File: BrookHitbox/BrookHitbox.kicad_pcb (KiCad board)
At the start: 2 copper layers, 15 parts

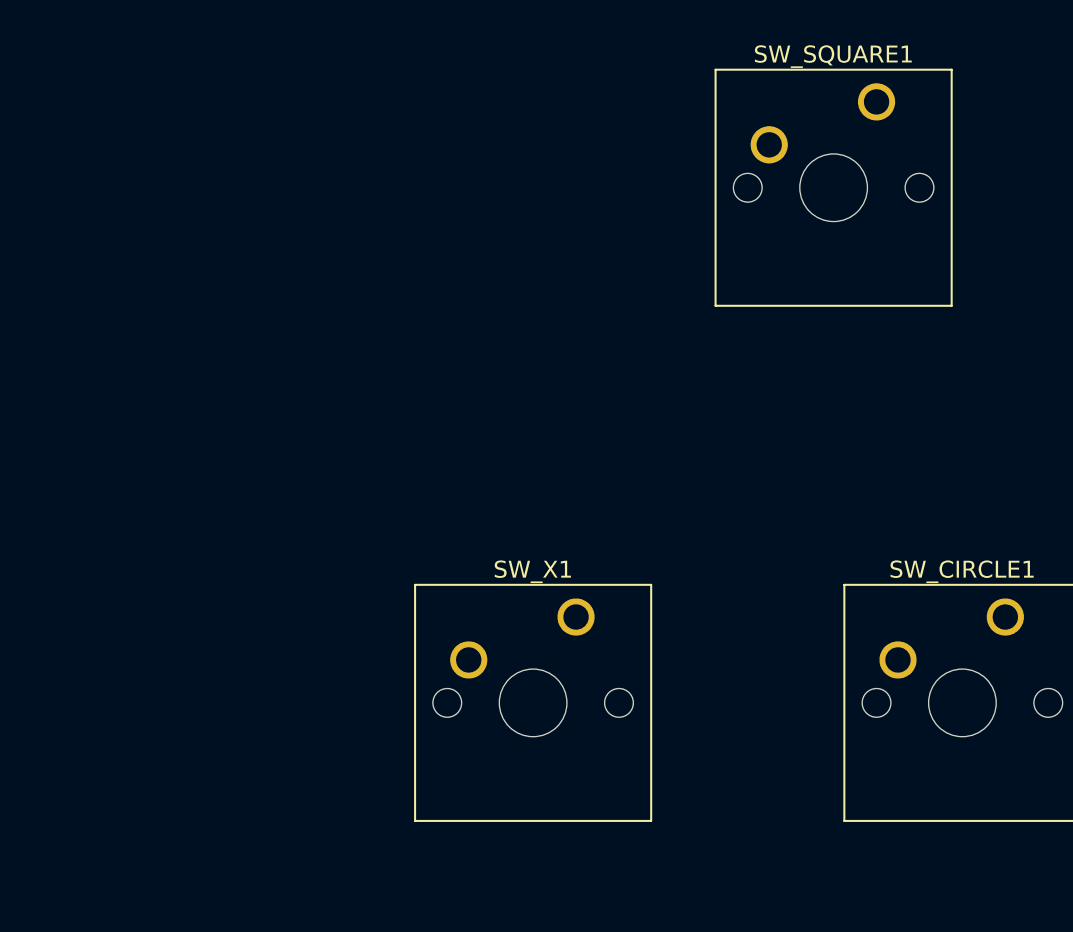
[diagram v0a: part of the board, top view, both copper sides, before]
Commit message: fix ERC errors, fix ratsnest not showing
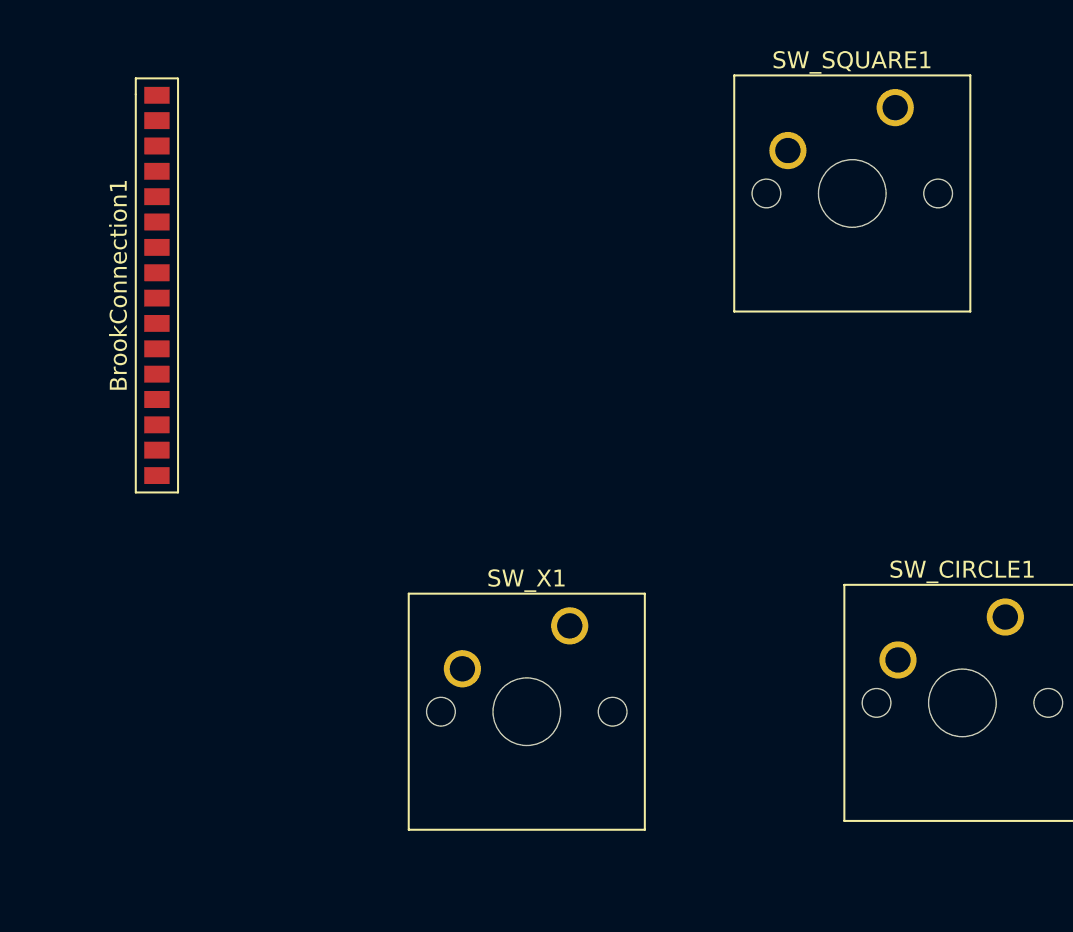
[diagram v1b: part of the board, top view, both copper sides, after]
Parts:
- added BrookConnection1: ~, BrookHitboxFootprints:BrookConn16, F.Cu at (155.5, 43.9)
- moved SW_SQUARE1 1.15 mm to (199.2, 33.4)
- moved SW_X1 0.64 mm to (180.0, 64.0)
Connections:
- SW_CIRCLE1 pad 1: (no net) -> /CIR
- SW_CIRCLE1 pad 2: (no net) -> GND
- SW_DOWN1 pad 1: (no net) -> /DWN
- SW_DOWN1 pad 2: (no net) -> GND
- SW_L1 pad 1: (no net) -> /L1
- SW_L1 pad 2: (no net) -> GND
- SW_L2 pad 1: (no net) -> /L2
- SW_L2 pad 2: (no net) -> GND
- SW_LEFT1 pad 1: (no net) -> /LFT
- SW_LEFT1 pad 2: (no net) -> GND
- SW_PSXBOX1 pad 1: (no net) -> /PS
- SW_PSXBOX1 pad 2: (no net) -> GND
- SW_R1 pad 1: (no net) -> /R1
- SW_R1 pad 2: (no net) -> GND
- SW_R2 pad 1: (no net) -> /R2
- SW_R2 pad 2: (no net) -> GND
- SW_RIGHT1 pad 1: (no net) -> /RT
- SW_RIGHT1 pad 2: (no net) -> GND
- SW_SELECT1 pad 1: (no net) -> /SEL
- SW_SELECT1 pad 2: (no net) -> GND
- SW_SQUARE1 pad 1: (no net) -> /SQU
- SW_SQUARE1 pad 2: (no net) -> GND
- SW_START1 pad 1: (no net) -> /STA
- SW_START1 pad 2: (no net) -> GND
- SW_TRIANGLE1 pad 1: (no net) -> /TRI
- SW_TRIANGLE1 pad 2: (no net) -> GND
- SW_UP1 pad 1: (no net) -> /UP
- SW_UP1 pad 2: (no net) -> GND
- SW_X1 pad 1: (no net) -> /X
- SW_X1 pad 2: (no net) -> GND

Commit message: update pcb layout
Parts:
- moved SW_L1 1.46 mm to (276.2, 31.5)
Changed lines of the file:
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@@
         (effects (font (size 1 1) (thickness 0.15)))
     )
-    (fp_text value "~" (at -2.54 12.954) (layer "F.Fab")
+    (fp_text value "~" (at -2.54 12.954) (layer "F.Fab") hide
         (effects (font (size 1 1) (thickness 0.15)))
     )
@@
         (effects (font (size 1 1) (thickness 0.15)))
     )
-    (fp_text value "~" (at -2.54 12.954) (layer "F.Fab")
+    (fp_text value "~" (at -2.54 12.954) (layer "F.Fab") hide
         (effects (font (size 1 1) (thickness 0.15)))
     )
@@
         (effects (font (size 1 1) (thickness 0.15)))
     )
-    (fp_text value "~" (at -2.54 12.954) (layer "F.Fab")
+    (fp_text value "~" (at -2.54 12.954) (layer "F.Fab") hide
         (effects (font (size 1 1) (thickness 0.15)))
     )
@@
         (effects (font (size 1 1) (thickness 0.15)))
     )
-    (fp_text value "~" (at -2.54 12.954) (layer "F.Fab")
+    (fp_text value "~" (at -2.54 12.954) (layer "F.Fab") hide
         (effects (font (size 1 1) (thickness 0.15)))
     )
@@
         (effects (font (size 1 1) (thickness 0.15)))
     )
-    (fp_text value "~" (at -2.54 12.954) (layer "F.Fab")
+    (fp_text value "~" (at -2.54 12.954) (layer "F.Fab") hide
         (effects (font (size 1 1) (thickness 0.15)))
     )
@@
         (effects (font (size 1 1) (thickness 0.15)))
     )
-    (fp_text value "~" (at -2.54 12.954) (layer "F.Fab")
+    (fp_text value "~" (at -2.54 12.954) (layer "F.Fab") hide
         (effects (font (size 1 1) (thickness 0.15)))
     )
@@
         (effects (font (size 1 1) (thickness 0.15)))
     )
-    (fp_text value "~" (at -2.54 12.954) (layer "F.Fab")
+    (fp_text value "~" (at -2.54 12.954) (layer "F.Fab") hide
         (effects (font (size 1 1) (thickness 0.15)))
     )
@@
         (effects (font (size 1 1) (thickness 0.15)))
     )
-    (fp_text value "~" (at -2.54 12.954) (layer "F.Fab")
+    (fp_text value "~" (at -2.54 12.954) (layer "F.Fab") hide
         (effects (font (size 1 1) (thickness 0.15)))
     )
@@
         (effects (font (size 1 1) (thickness 0.15)))
     )
-    (fp_text value "~" (at -2.54 12.954) (layer "F.Fab")
+    (fp_text value "~" (at -2.54 12.954) (layer "F.Fab") hide
         (effects (font (size 1 1) (thickness 0.15)))
     )
@@
         (effects (font (size 1 1) (thickness 0.15)))
     )
-    (fp_text value "~" (at -2.54 12.954) (layer "F.Fab")
+    (fp_text value "~" (at -2.54 12.954) (layer "F.Fab") hide
         (effects (font (size 1 1) (thickness 0.15)))
     )
@@
         (effects (font (size 1 1) (thickness 0.15)))
     )
-    (fp_text value "~" (at -2.54 12.954) (layer "F.Fab")
+    (fp_text value "~" (at -2.54 12.954) (layer "F.Fab") hide
         (effects (font (size 1 1) (thickness 0.15)))
     )
@@
         (effects (font (size 1 1) (thickness 0.15)))
     )
-    (fp_text value "~" (at -2.54 12.954) (layer "F.Fab")
+    (fp_text value "~" (at -2.54 12.954) (layer "F.Fab") hide
         (effects (font (size 1 1) (thickness 0.15)))
     )
@@
         (effects (font (size 1 1) (thickness 0.15)))
     )
-    (fp_text value "~" (at -2.54 12.954) (layer "F.Fab")
+    (fp_text value "~" (at -2.54 12.954) (layer "F.Fab") hide
         (effects (font (size 1 1) (thickness 0.15)))
     )
@@
         (effects (font (size 1 1) (thickness 0.15)))
     )
-    (fp_text value "~" (at 0 -2.25 90) (layer "F.Fab")
+    (fp_text value "~" (at -2.714 -2.986 90) (layer "F.Fab") hide
         (effects (font (size 1 1) (thickness 0.15)))
     )
@@
   )
   (footprint "Button_Switch_Keyboard:SW_Cherry_MX_1.00u_PCB" (layer "F.Cu")
-    (at 275.664 32.82)
+    (at 276.234 31.475)
     (descr "Cherry MX keyswitch, 1.00u, PCB mount, http://cherryamericas.com/wp-content/uploads/2014/12/mx_cat.pdf")
     (tags "Cherry MX keyswitch 1.00u PCB")
@@
         (effects (font (size 1 1) (thickness 0.15)))
     )
-    (fp_text value "~" (at -2.54 12.954) (layer "F.Fab")
+    (fp_text value "~" (at -2.54 12.954) (layer "F.Fab") hide
         (effects (font (size 1 1) (thickness 0.15)))
     )
@@
         (effects (font (size 1 1) (thickness 0.15)))
     )
-    (fp_text value "~" (at -2.54 12.954) (layer "F.Fab")
-        (effects (font (size 1 1) (thickness 0.15)))
-    )
+    (fp_text value "~" (at -2.54 12.954) (layer "F.Fab") hide
+        (effects (font (size 1 1) (thickness 0.15)))
+    )

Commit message: pcb layout placement for buttons
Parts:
- moved SW_L2 60.6 mm to (309.1, 88.8)
- moved SW_R2 55.0 mm to (282.8, 72.8)
- moved SW_X1 51.2 mm to (228.0, 81.8)
- moved SW_PSXBOX1 49.9 mm to (198.3, 165.1)
- moved SW_CIRCLE1 49.1 mm to (254.5, 69.8)
- moved SW_L1 44.3 mm to (309.1, 61.2)
- moved SW_START1 42.4 mm to (148.9, 82.2)
- moved SW_RIGHT1 39.3 mm to (69.2, 82.2)
- moved SW_SQUARE1 35.5 mm to (228.0, 54.2)
- moved SW_R1 33.6 mm to (282.8, 45.1)
- moved SW_LEFT1 33.2 mm to (14.2, 73.1)
- moved SW_TRIANGLE1 29.9 mm to (254.5, 42.2)
- moved SW_DOWN1 29.3 mm to (42.6, 70.4)
- moved SW_SELECT1 26.6 mm to (198.3, 133.9)
- moved SW_UP1 24.8 mm to (76.1, 149.3)
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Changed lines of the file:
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@@
   (net 16 "GND")
   (footprint "Button_Switch_Keyboard:SW_Cherry_MX_1.00u_PCB" (layer "F.Cu")
-    (at 226.06 33.02)
+    (at 254.4861 42.1726)
     (descr "Cherry MX keyswitch, 1.00u, PCB mount, http://cherryamericas.com/wp-content/uploads/2014/12/mx_cat.pdf")
     (tags "Cherry MX keyswitch 1.00u PCB")
@@
   )
   (footprint "Button_Switch_Keyboard:SW_Cherry_MX_1.00u_PCB" (layer "F.Cu")
-    (at 185.42 116.84)
+    (at 198.2661 165.0726)
     (descr "Cherry MX keyswitch, 1.00u, PCB mount, http://cherryamericas.com/wp-content/uploads/2014/12/mx_cat.pdf")
     (tags "Cherry MX keyswitch 1.00u PCB")
@@
   )
   (footprint "Button_Switch_Keyboard:SW_Cherry_MX_1.00u_PCB" (layer "F.Cu")
-    (at 208.28 109.22)
+    (at 198.2661 133.8876)
     (descr "Cherry MX keyswitch, 1.00u, PCB mount, http://cherryamericas.com/wp-content/uploads/2014/12/mx_cat.pdf")
     (tags "Cherry MX keyswitch 1.00u PCB")
@@
   )
   (footprint "Button_Switch_Keyboard:SW_Cherry_MX_1.00u_PCB" (layer "F.Cu")
-    (at 199.224 33.359)
+    (at 227.9681 54.1686)
     (descr "Cherry MX keyswitch, 1.00u, PCB mount, http://cherryamericas.com/wp-content/uploads/2014/12/mx_cat.pdf")
     (tags "Cherry MX keyswitch 1.00u PCB")
@@
   )
   (footprint "Button_Switch_Keyboard:SW_Cherry_MX_1.00u_PCB" (layer "F.Cu")
-    (at 251.46 33.02)
+    (at 282.8411 45.1476)
     (descr "Cherry MX keyswitch, 1.00u, PCB mount, http://cherryamericas.com/wp-content/uploads/2014/12/mx_cat.pdf")
     (tags "Cherry MX keyswitch 1.00u PCB")
@@
   )
   (footprint "Button_Switch_Keyboard:SW_Cherry_MX_1.00u_PCB" (layer "F.Cu")
-    (at 205.74 63.5)
+    (at 254.4861 69.7826)
     (descr "Cherry MX keyswitch, 1.00u, PCB mount, http://cherryamericas.com/wp-content/uploads/2014/12/mx_cat.pdf")
     (tags "Cherry MX keyswitch 1.00u PCB")
@@
   )
   (footprint "Button_Switch_Keyboard:SW_Cherry_MX_1.00u_PCB" (layer "F.Cu")
-    (at 58.42 45.72)
+    (at 42.6021 70.3886)
     (descr "Cherry MX keyswitch, 1.00u, PCB mount, http://cherryamericas.com/wp-content/uploads/2014/12/mx_cat.pdf")
     (tags "Cherry MX keyswitch 1.00u PCB")
@@
   )
   (footprint "Button_Switch_Keyboard:SW_Cherry_MX_1.00u_PCB" (layer "F.Cu")
-    (at 254 63.5)
+    (at 309.0641 88.7936)
     (descr "Cherry MX keyswitch, 1.00u, PCB mount, http://cherryamericas.com/wp-content/uploads/2014/12/mx_cat.pdf")
     (tags "Cherry MX keyswitch 1.00u PCB")
@@
   )
   (footprint "Button_Switch_Keyboard:SW_Cherry_MX_1.00u_PCB" (layer "F.Cu")
-    (at 83.82 45.72)
+    (at 69.1741 82.1516)
     (descr "Cherry MX keyswitch, 1.00u, PCB mount, http://cherryamericas.com/wp-content/uploads/2014/12/mx_cat.pdf")
     (tags "Cherry MX keyswitch 1.00u PCB")
@@
   )
   (footprint "Button_Switch_Keyboard:SW_Cherry_MX_1.00u_PCB" (layer "F.Cu")
-    (at 33.02 45.72)
+    (at 14.2461 73.1146)
     (descr "Cherry MX keyswitch, 1.00u, PCB mount, http://cherryamericas.com/wp-content/uploads/2014/12/mx_cat.pdf")
     (tags "Cherry MX keyswitch 1.00u PCB")
@@
   )
   (footprint "Button_Switch_Keyboard:SW_Cherry_MX_1.00u_PCB" (layer "F.Cu")
-    (at 132.08 43.18)
+    (at 148.9061 82.1516)
     (descr "Cherry MX keyswitch, 1.00u, PCB mount, http://cherryamericas.com/wp-content/uploads/2014/12/mx_cat.pdf")
     (tags "Cherry MX keyswitch 1.00u PCB")
@@
   )
   (footprint "Button_Switch_Keyboard:SW_Cherry_MX_1.00u_PCB" (layer "F.Cu")
-    (at 228.6 63.5)
+    (at 282.8411 72.7576)
     (descr "Cherry MX keyswitch, 1.00u, PCB mount, http://cherryamericas.com/wp-content/uploads/2014/12/mx_cat.pdf")
     (tags "Cherry MX keyswitch 1.00u PCB")
@@
   )
   (footprint "Button_Switch_Keyboard:SW_Cherry_MX_1.00u_PCB" (layer "F.Cu")
-    (at 179.965 64.022)
+    (at 227.9681 81.7776)
     (descr "Cherry MX keyswitch, 1.00u, PCB mount, http://cherryamericas.com/wp-content/uploads/2014/12/mx_cat.pdf")
     (tags "Cherry MX keyswitch 1.00u PCB")
@@
   )
   (footprint "BrookHitboxFootprints:BrookConn16" (layer "F.Cu")
-    (at 155.54 43.879 -90)
+    (at 167.74 52.1 -90)
     (property "Sheetfile" "BrookHitbox.kicad_sch")
     (property "Sheetname" "")
@@
   )
   (footprint "Button_Switch_Keyboard:SW_Cherry_MX_1.00u_PCB" (layer "F.Cu")
-    (at 276.234 31.475)
+    (at 309.0641 61.1836)
     (descr "Cherry MX keyswitch, 1.00u, PCB mount, http://cherryamericas.com/wp-content/uploads/2014/12/mx_cat.pdf")
     (tags "Cherry MX keyswitch 1.00u PCB")
@@
   )
   (footprint "Button_Switch_Keyboard:SW_Cherry_MX_1.00u_PCB" (layer "F.Cu")
-    (at 76.2 124.46)
-    (descr "Cherry MX keyswitch, 1.00u, PCB mount, http://cherryamericas.com/wp-content/uploads/2014/12/mx_cat.pdf")
-    (tags "Cherry MX keyswitch 1.00u PCB")
+    (at 76.1331 149.3026)
+    (descr "Cherry MX keyswitch, 1.00u, PCB mount, http://cherryamericas.com/wp-content/uploads/2014/12/mx_cat.pdf")
+    (tags "Cherry MX keyswitch 1.00u PCB")

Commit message: add mounting holes
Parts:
- added H1: MountingHole, MountingHole:MountingHole_2.2mm_M2, F.Cu at (93.3, 55.8)
- added H2: MountingHole, MountingHole:MountingHole_2.2mm_M2, F.Cu at (95.5, 70.6)
- added H3: MountingHole, MountingHole:MountingHole_2.2mm_M2, F.Cu at (104.7, 55.9)
- added H4: MountingHole, MountingHole:MountingHole_2.2mm_M2, F.Cu at (106.6, 73.9)
- added H5: MountingHole, MountingHole:MountingHole_2.2mm_M2, F.Cu at (114.0, 56.8)
- added H6: MountingHole, MountingHole:MountingHole_2.2mm_M2, F.Cu at (115.2, 73.2)
- added H7: MountingHole, MountingHole:MountingHole_2.2mm_M2, F.Cu at (127.8, 56.6)
- added H8: MountingHole, MountingHole:MountingHole_2.2mm_M2, F.Cu at (130.3, 71.3)
- moved SW_R1 60.2 mm to (335.0, 75.3)
- moved SW_R2 60.2 mm to (335.0, 102.9)
- moved SW_CIRCLE1 60.2 mm to (306.6, 99.9)
- moved SW_PSXBOX1 60.2 mm to (250.4, 195.2)
- moved SW_RIGHT1 60.2 mm to (121.3, 112.3)
- moved SW_SELECT1 60.2 mm to (250.4, 164.0)
- moved SW_TRIANGLE1 60.2 mm to (306.6, 72.3)
- moved SW_DOWN1 60.2 mm to (94.7, 100.5)
- moved SW_LEFT1 60.2 mm to (66.4, 103.2)
- moved SW_UP1 60.2 mm to (128.3, 179.4)
- moved BrookConnection1 60.2 mm to (219.9, 82.2)
- moved SW_L1 60.2 mm to (361.2, 91.3)
- moved SW_L2 60.2 mm to (361.2, 118.9)
- moved SW_SQUARE1 60.2 mm to (280.1, 84.3)
- moved SW_START1 60.2 mm to (201.0, 112.3)
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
